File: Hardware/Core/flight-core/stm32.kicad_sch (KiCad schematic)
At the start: 14 parts, among them J6 USB_C_Receptacle, SW1 SW_SPDT, SW2 SW_MEC_5E, U1 STM32G473CCTx, U3 USBLC6-2SC6, Y1 48 MHZ

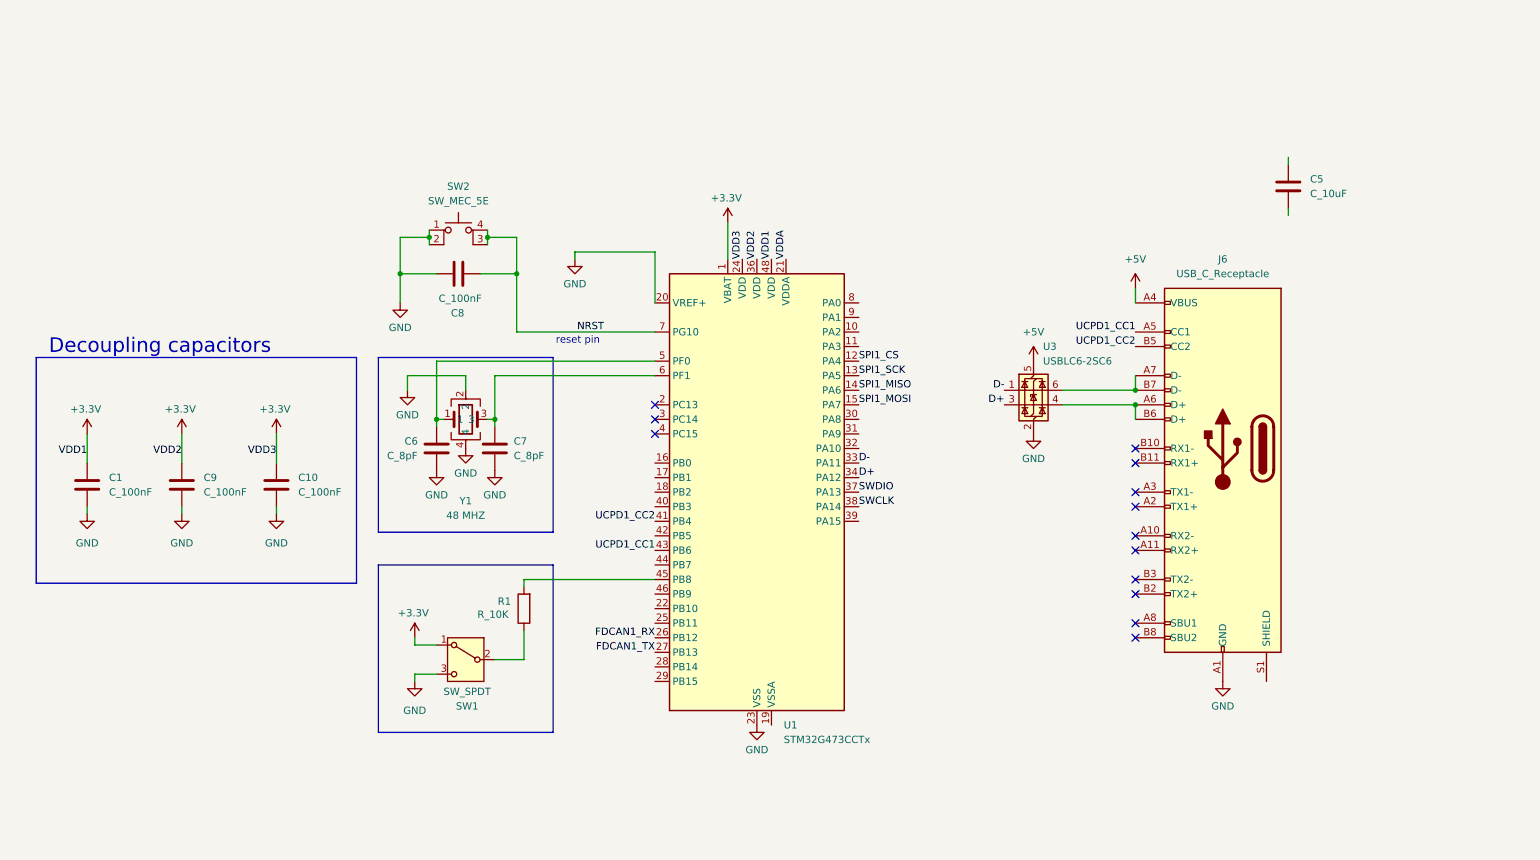
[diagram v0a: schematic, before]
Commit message: added many shutdown nodes, can_repeater instances, separated arm_connectors, basic stm32 peripherals
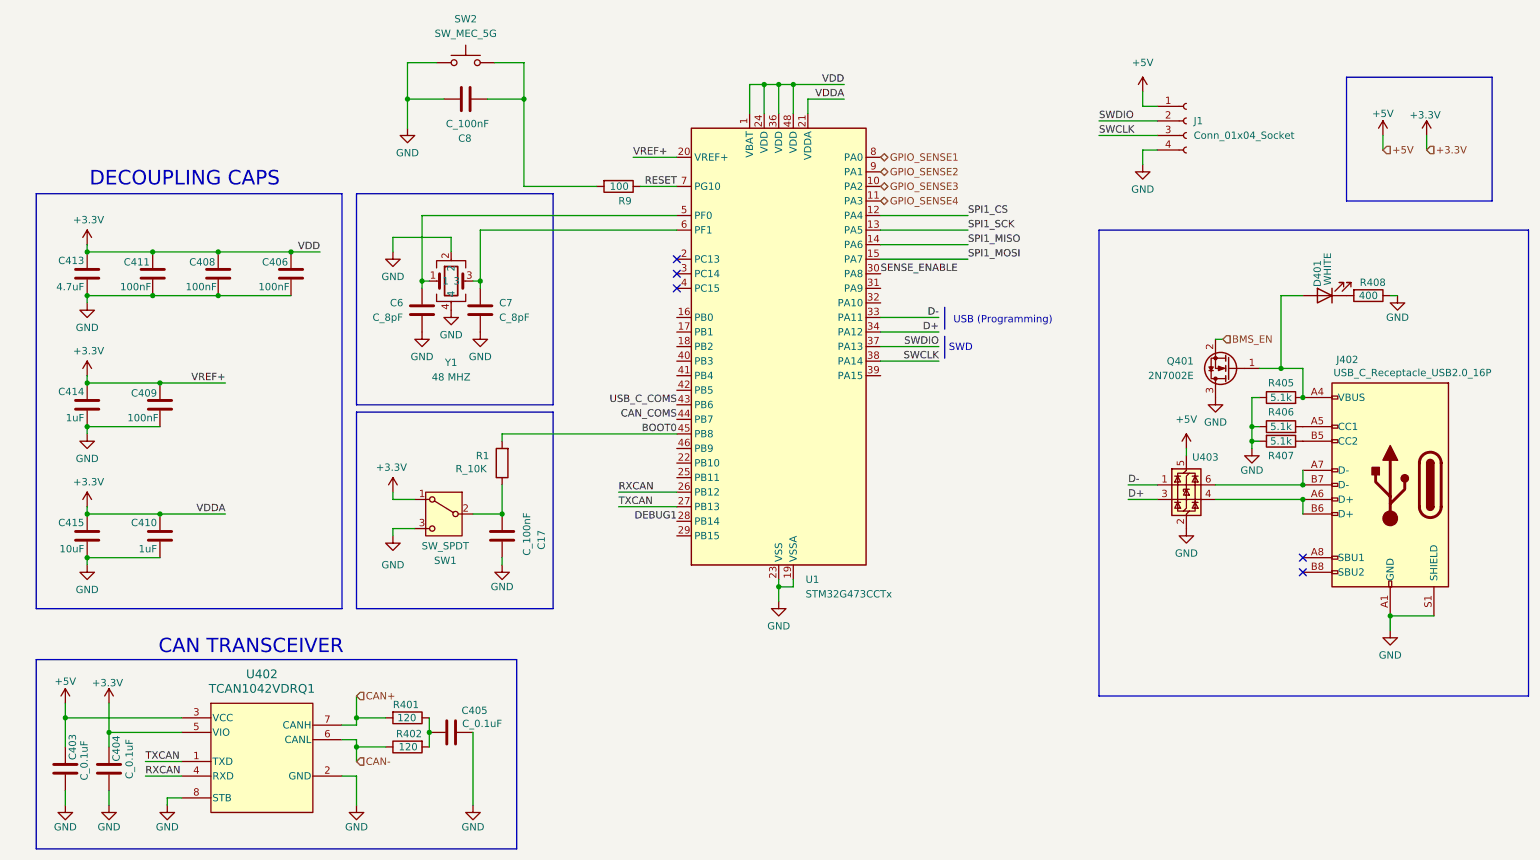
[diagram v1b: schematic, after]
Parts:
- removed C1, C10, C9: C_100nF, footprints:C_0603_1608Metric, symbol formula:C_100nF
- removed J6: USB_C_Receptacle, Connector_USB:USB_C_Receptacle_Molex_105450-0101, symbol Connector:USB_C_Receptacle
- removed SW2: SW_MEC_5E, symbol Switch:SW_MEC_5E
- removed U3: USBLC6-2SC6, Package_TO_SOT_SMD:SOT-23-6, symbol Power_Protection:USBLC6-2SC6
- added C17: C_100nF, OEM:C_0603_1608Metric, symbol formula:C_100nF
- added C403, C404, C405: C_0.1uF, OEM:C_0603_1608Metric, symbol OEM:0u1F
- added C406, C408, C409, C411: 100nF, Capacitor_SMD:C_0603_1608Metric, symbol formula:C_100nF
- added C410: 1uF, Capacitor_SMD:C_0603_1608Metric, symbol formula:C_10uF
- added C413: 4.7uF, Capacitor_SMD:C_0805_2012Metric, symbol formula:C_10uF
- added C415: 10uF, Capacitor_SMD:C_0805_2012Metric, symbol formula:C_10uF
- added D401: WHITE, LED_SMD:LED_0805_2012Metric, symbol Device:LED
- added J1: Conn_01x04_Socket, Connector_PinSocket_2.54mm:PinSocket_1x04_P2.54mm_Vertical, symbol Connector:Conn_01x04_Socket
- added J402: USB_C_Receptacle_USB2.0_16P, Connector_USB:USB_C_Receptacle_G-Switch_GT-USB-7051x, symbol Connector:USB_C_Receptacle_USB2.0_16P
- added Q401: 2N7002E, Package_TO_SOT_SMD:SOT-23, symbol Transistor_FET:2N7002E
- added R401, R402: 120, OEM:R_0603_1608Metric, symbol OEM:120R_DNP
- added R405, R406, R407: 5.1k, OEM:R_0603_1608Metric, symbol OEM:1KR
- added R408: 400, Resistor_SMD:R_0603_1608Metric, symbol Device:R
- added R9: 100, footprints:R_0805_OEM, symbol formula:R_10K
- added SW2: SW_MEC_5G, Button_Switch_SMD:SW_MEC_5GSH9, symbol Switch:SW_MEC_5G
- added U402: TCAN1042VDRQ1, BAD_LIB:D0008A_M, symbol OlinBAD:TCAN1042VDRQ1
- added U403: USBLC6-2SC6, Package_TO_SOT_SMD:SOT-23-6, symbol Power_Protection:USBLC6-2SC6
- C414: renamed from C5; value C_10uF -> 1uF; footprint footprints:C_0805_OEM -> Capacitor_SMD:C_0603_1608Metric
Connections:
- net VDDA is gone; now on net +3.3V: U1.21 (VDDA)
- net +3.3V: now also C414.1, U1.20 (VREF+), C404.1, C406.1, C408.1, C409.1, C410.1, C411.1, C413.1, C415.1, U402.5 (VIO)
- net +5V: now also C403.1, J1.1 (Pin_1), U402.3 (VCC), U403.5 (VBUS)
- net D+: now also U403.3 (I/O2)
- net D-: now also U403.1 (I/O1)
- net GND: now also C414.2, U1.19 (VSSA), C17.1, C403.2, C404.2, C405.2, C406.2, C408.2, C409.2, C410.2, C411.2, C413.2, C415.2, J1.4 (Pin_4), J402.A1 (GND), J402.A12 (GND), J402.B1 (GND), J402.B12 (GND), J402.S1 (SHIELD), Q401.3 (D), R405.1, R406.1, R407.2, R408.1, SW2.1 (A), SW2.2 (A), U402.2 (GND), U402.8 (STB), U403.2 (GND); no longer U1.20 (VREF+)
- net SWCLK: now also J1.3 (Pin_3)
- net SWDIO: now also J1.2 (Pin_2)
- net GPIO_SENSE3: now reaches U1.10 (PA2)
- net GPIO_SENSE4: now reaches U1.11 (PA3)
- net DEBUG1: now reaches U1.28 (PB14)
- net SENSE_ENABLE: now reaches U1.30 (PA8)
- net CAN_COMS: now reaches U1.44 (PB7)
- net BOOT0: now reaches R1.2, U1.45 (PB8)
- net GPIO_SENSE1: now reaches U1.8 (PA0)
- net GPIO_SENSE2: now reaches U1.9 (PA1)
- net at R1.1, SW1.2 (B): now also C17.2
- net FDCAN1_RX renamed RXCAN
- net RXCAN: now also U402.4 (RXD)
- net FDCAN1_TX renamed TXCAN
- net TXCAN: now also U402.1 (TXD)
- net NRST: no longer names the net of C8.2
- net NRST: now also R9.2, SW2.3 (B), SW2.4 (B); no longer U1.7 (PG10)
- net UCPD1_CC1 renamed USB_C_COMS
- net UCPD1_CC2: no longer names the net of U1.41 (PB4)
- new net: D401.1 (K), R408.2
- new net: D401.2 (A), J402.A4 (VBUS), J402.A9 (VBUS), J402.B4 (VBUS), J402.B9 (VBUS), Q401.1 (G), R405.2
- new net: J402.A6 (D+), J402.B6 (D+), U403.4 (I/O2)
- new net: J402.A7 (D-), J402.B7 (D-), U403.6 (I/O1)
- new net: C405.1, R401.1, R402.2
- new net: J402.A5 (CC1), R406.2
- new net: J402.B5 (CC2), R407.1
- new net BMS_EN: Q401.2 (S)
- new net CAN+: R401.2, U402.7 (CANH)
- new net CAN-: R402.1, U402.6 (CANL)
- new net RESET: R9.1, U1.7 (PG10)
- no-connect marks 13 -> 5
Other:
- note added: "CAN TRANSCEIVER"
- note added: "DECOUPLING CAPS"
- note added: "SWD"
- note added: "USB (Programming)"
- note removed: "Decoupling capacitors"
- note removed: "reset pin"
- moved on the sheet: C414, C8, R1, SW1

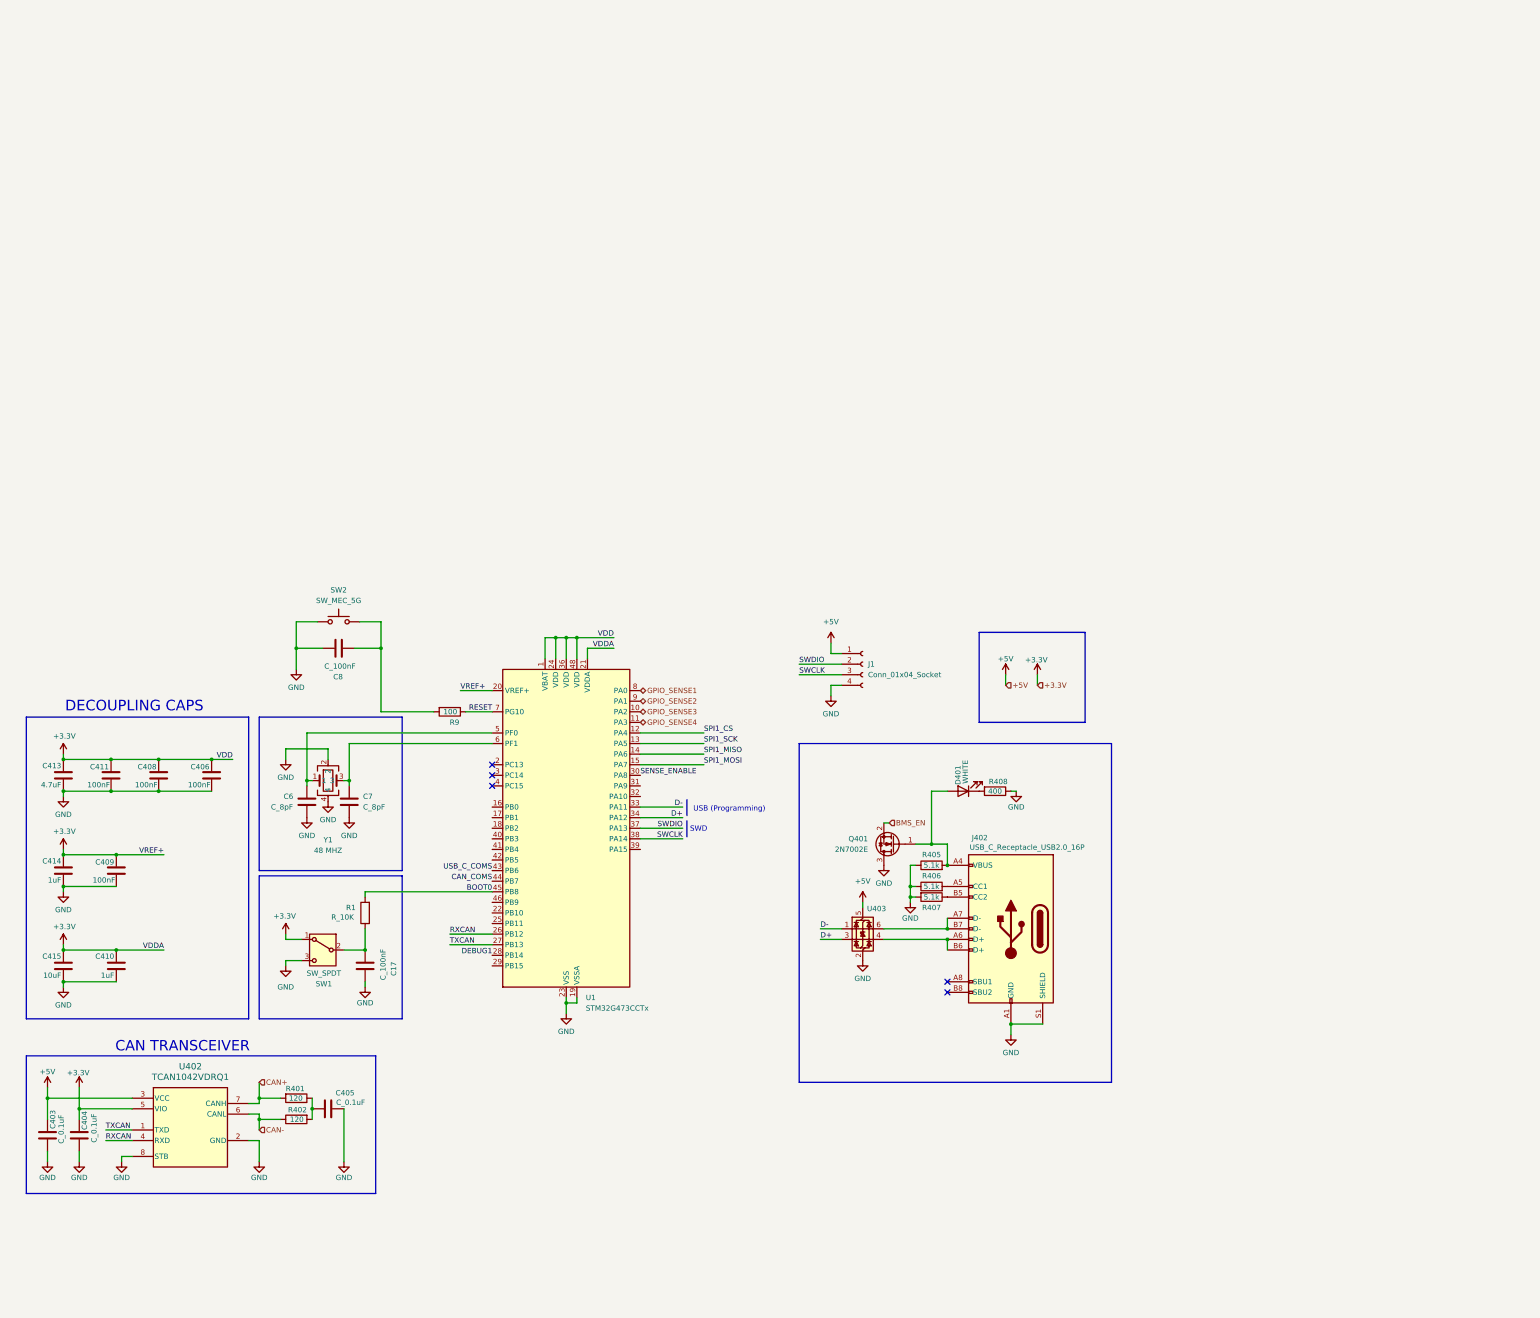
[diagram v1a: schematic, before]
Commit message: renaming the values of LRC generics to just the value with unit letter (except resistors are just the value)
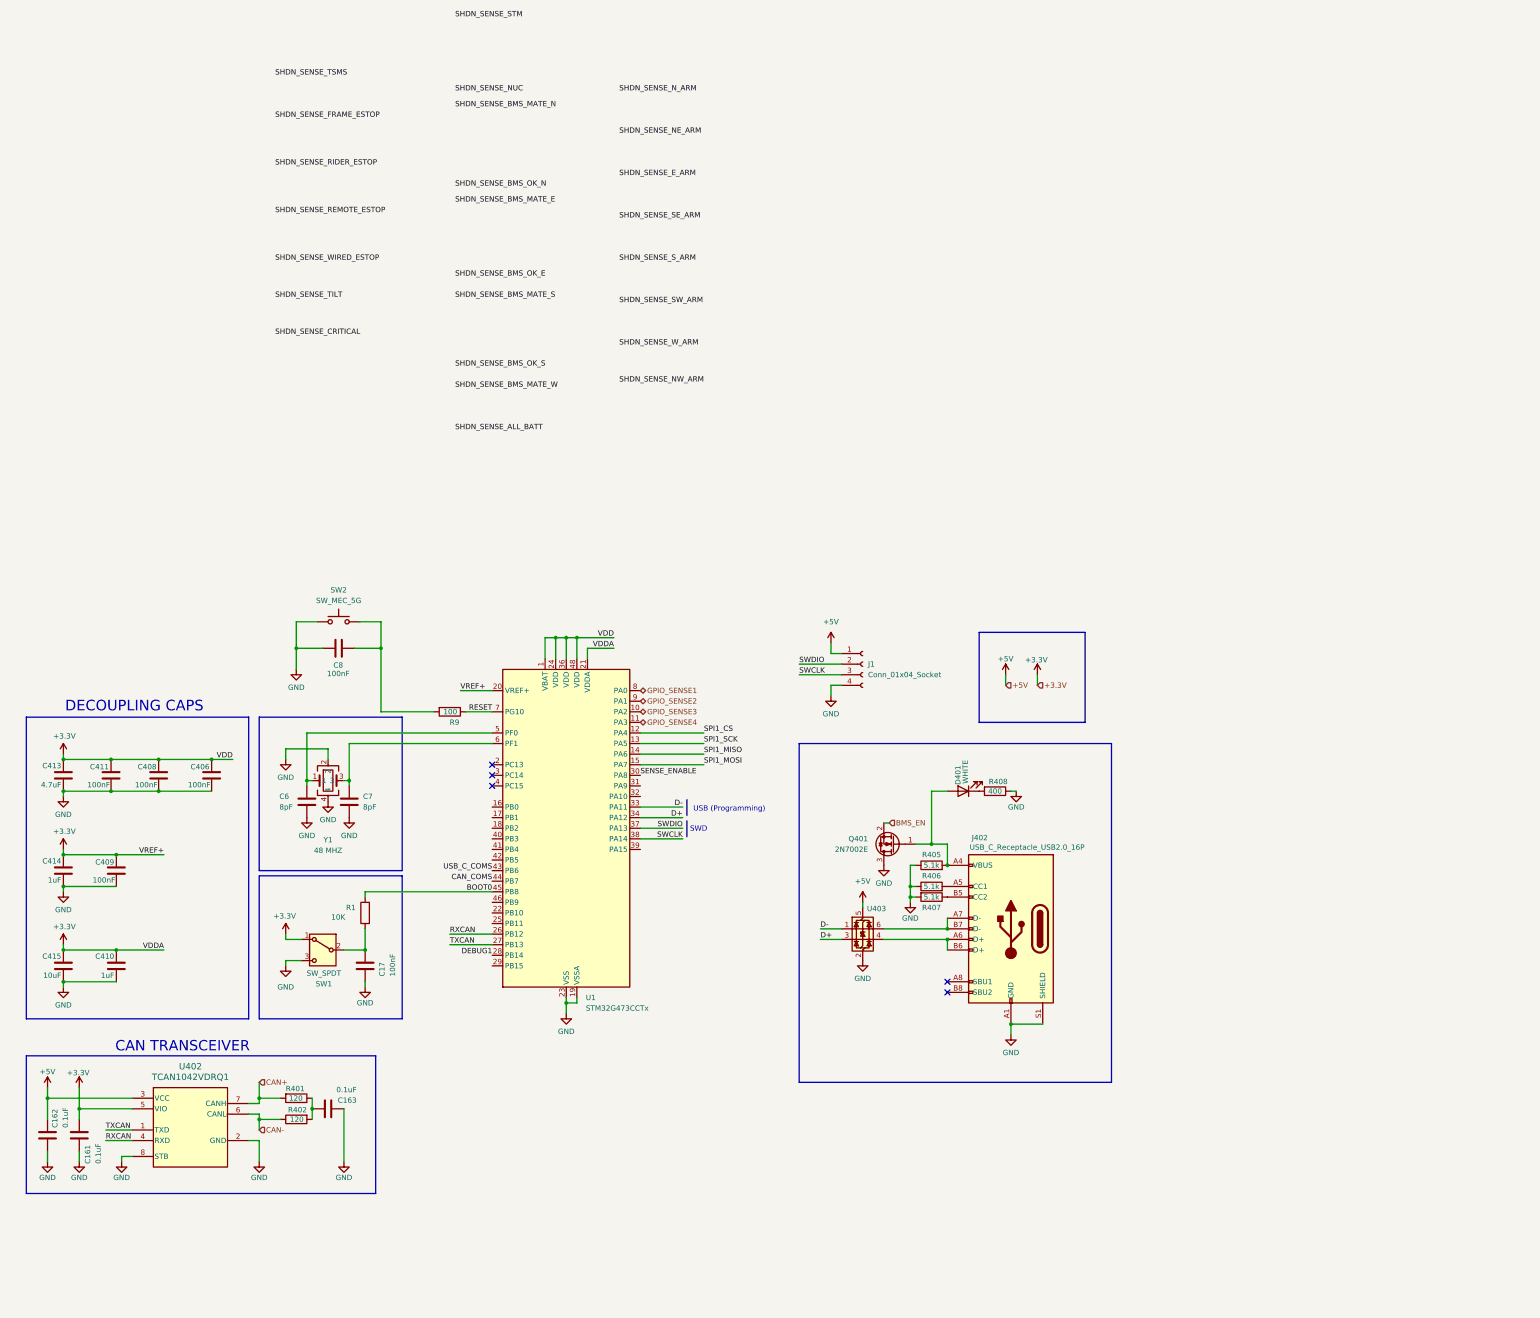
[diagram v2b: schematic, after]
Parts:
- removed C403, C404, C405: C_0.1uF, OEM:C_0603_1608Metric, symbol OEM:0u1F
- removed C6, C7: C_8pF, footprints:C_0603_1608Metric, symbol formula:C_100nF
- added C161, C162, C163: 0.1uF, footprints:C_0603_1608Metric, symbol OlinBAD:C_0.1uF_0603
- added C6, C7: 8pF, footprints:C_0603_1608Metric, symbol Device:C
- C17: value C_100nF -> 100nF; footprint OEM:C_0603_1608Metric -> footprints:C_0603_1608Metric
- C8: value C_100nF -> 100nF; footprint footprints:C_0603_1608Metric -> Capacitor_SMD:C_0603_1608Metric
- R1: value R_10K -> 10K
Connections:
- net +3.3V: now also C161.1
- net +5V: now also C162.1
- net GND: now also C17.2, C161.2, C162.2, C163.2, C6.2, C7.2; no longer C17.1
- net at U1.5 (PF0), Y1.1: now also C6.1
- net at U1.6 (PF1), Y1.3: now also C7.1
- net at R401.1, R402.2: now also C163.1
- net at R1.1, SW1.2 (B): now also C17.1; no longer C17.2
